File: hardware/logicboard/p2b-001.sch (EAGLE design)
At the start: 70 parts, among them IC1 74LS06N, IC2 4066N, J1 MKR, J2 GPIO, J3 Vcc, J4 RLY, J42 RLY2, J5 SPI, J6 LED, J7 DIN5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

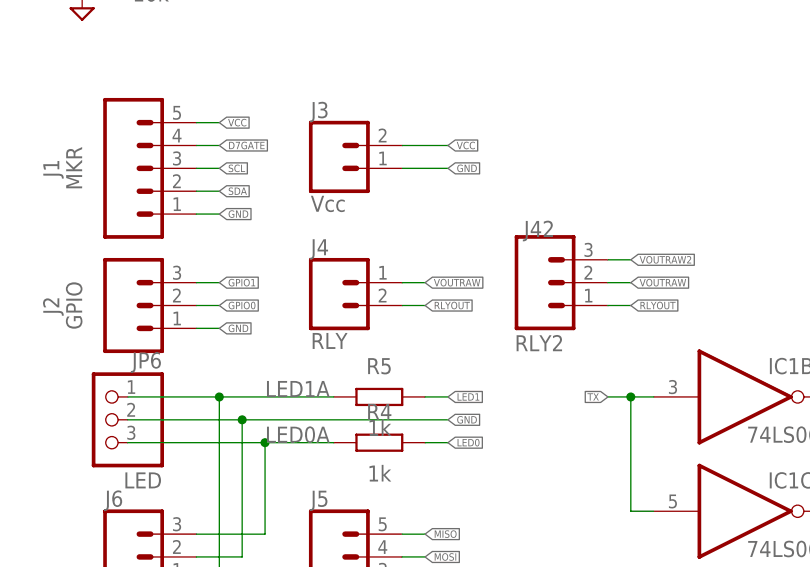
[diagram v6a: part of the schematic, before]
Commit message: J4 is now 3-pin.
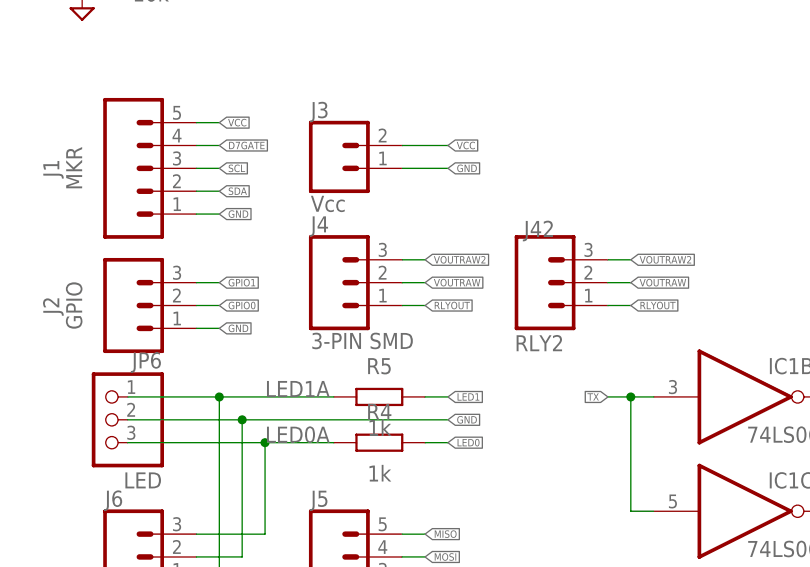
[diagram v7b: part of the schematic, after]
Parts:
- J4: value RLY -> 3-PIN SMD; device SparkFun-Connectors:CONN_02-JST-2MM-SMT -> SparkFun-Connectors:CONN_03JST-SMD
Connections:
- net VOUTRAW2: now also J4.3
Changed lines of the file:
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@@
 <part name="X14" library="wirepad" library_urn="urn:adsk.eagle:library:412" deviceset="PAD-N" device=""/>
 <part name="JP1" library="pinhead" library_urn="urn:adsk.eagle:library:325" deviceset="PINHD-2X3" device="" package3d_urn="urn:adsk.eagle:package:22462/2" value="PWRSEL"/>
-<part name="J4" library="SparkFun-Connectors" library_urn="urn:adsk.eagle:library:513" deviceset="CONN_02" device="-JST-2MM-SMT" package3d_urn="urn:adsk.eagle:package:38042/1" value="RLY"/>
 <part name="J3" library="SparkFun-Connectors" library_urn="urn:adsk.eagle:library:513" deviceset="CONN_02" device="JST-PTH-2" package3d_urn="urn:adsk.eagle:package:38053/1" value="Vcc"/>
 <part name="J5" library="SparkFun-Connectors" library_urn="urn:adsk.eagle:library:513" deviceset="CONN_05" device="JST-VERT" package3d_urn="urn:adsk.eagle:package:38111/1" value="SPI"/>
@@
 <part name="SUPPLY25" library="supply2" library_urn="urn:adsk.eagle:library:372" deviceset="VCC" device=""/>
 <part name="J42" library="SparkFun-Connectors" library_urn="urn:adsk.eagle:library:513" deviceset="CONN_03" device="JST-PTH" package3d_urn="urn:adsk.eagle:package:38069/1" value="RLY2"/>
+<part name="J4" library="SparkFun-Connectors" library_urn="urn:adsk.eagle:library:513" deviceset="CONN_03" device="JST-SMD" package3d_urn="urn:adsk.eagle:package:38075/1" value="3-PIN SMD"/>
 </parts>
 <sheets>
@@
 <attribute name="VALUE" x="77.47" y="226.06" size="1.778" layer="96"/>
 </instance>
-<instance part="J4" gate="G$1" x="88.9" y="48.26" smashed="yes">
-<attribute name="VALUE" x="86.36" y="43.434" size="1.778" layer="96" font="vector"/>
-<attribute name="NAME" x="86.36" y="53.848" size="1.778" layer="95" font="vector"/>
-</instance>
 <instance part="J3" gate="G$1" x="88.9" y="63.5" smashed="yes">
 <attribute name="VALUE" x="86.36" y="58.674" size="1.778" layer="96" font="vector"/>
@@
 <attribute name="VALUE" x="111.76" y="43.18" size="1.778" layer="96" align="bottom-center"/>
 <attribute name="NAME" x="111.76" y="55.88" size="1.778" layer="95" align="bottom-center"/>
+</instance>
+<instance part="J4" gate="J$1" x="88.9" y="50.8" smashed="yes">
+<attribute name="VALUE" x="86.36" y="43.434" size="1.778" layer="96" font="vector"/>
+<attribute name="NAME" x="86.36" y="56.388" size="1.778" layer="95" font="vector"/>
 </instance>
 </instances>
@@
 <pinref part="J42" gate="J$1" pin="3"/>
 </segment>
+<segment>
+<pinref part="J4" gate="J$1" pin="3"/>
+<wire x1="96.52" y1="53.34" x2="99.06" y2="53.34" width="0.1524" layer="91"/>
+<label x="99.06" y="53.34" size="0.8128" layer="95" xref="yes"/>
+</segment>
 </net>
 <net name="VOUT" class="4">
@@
 <wire x1="96.52" y1="50.8" x2="99.06" y2="50.8" width="0.1524" layer="91"/>
 <label x="99.06" y="50.8" size="0.8128" layer="95" xref="yes"/>
-<pinref part="J4" gate="G$1" pin="2"/>
+<pinref part="J4" gate="J$1" pin="2"/>
 </segment>
 <segment>
@@
 <wire x1="96.52" y1="48.26" x2="99.06" y2="48.26" width="0.1524" layer="91"/>
 <label x="99.06" y="48.26" size="0.8128" layer="95" xref="yes"/>
-<pinref part="J4" gate="G$1" pin="1"/>
-</segment>
-<segment>
+<pinref part="J4" gate="J$1" pin="1"/>
+</segment>
+<segment>

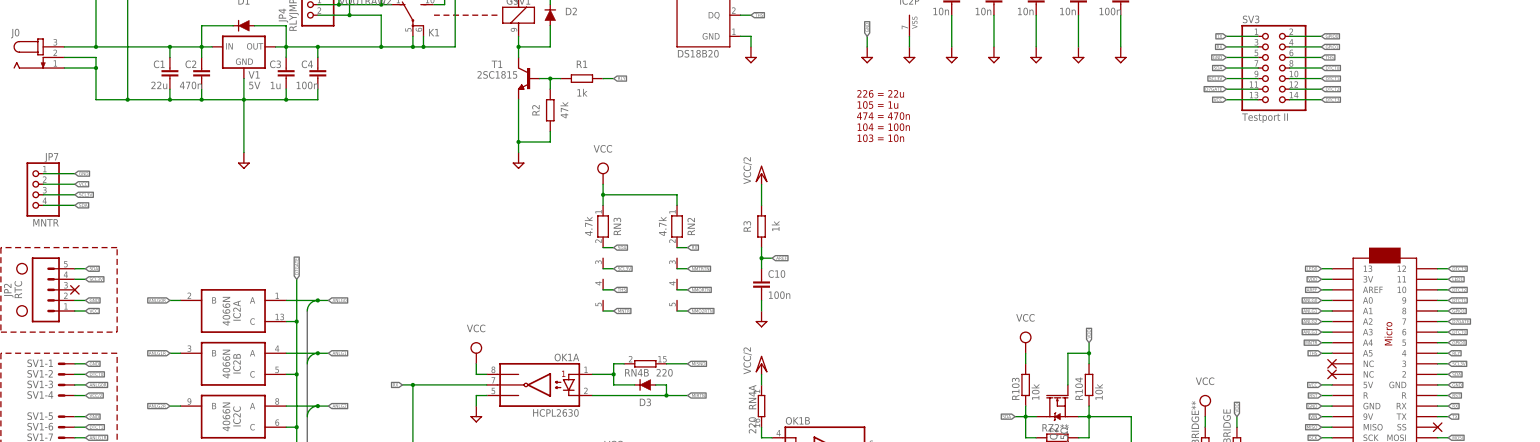
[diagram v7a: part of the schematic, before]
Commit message: Fixed SCL signal.
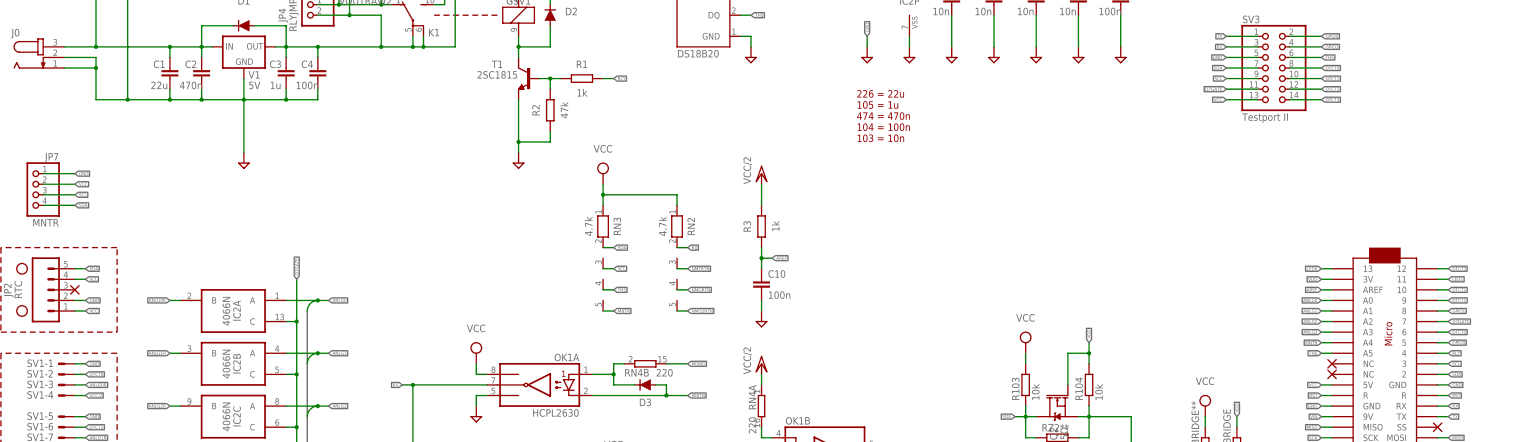
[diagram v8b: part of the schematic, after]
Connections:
- net SCL: now also JP2.4, JP7.3, MC1.3, RN3.3, SV3.9
- net SCL3V: no longer JP2.4, JP7.3, MC1.3, RN3.3, SV3.9
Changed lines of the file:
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@@
-</segment>
-</net>
-<net name="SCL3V" class="0">
-<segment>
-<pinref part="MC1" gate="G$1" pin="3"/>
-<wire x1="368.3" y1="124.46" x2="370.84" y2="124.46" width="0.1524" layer="91"/>
-<label x="370.84" y="124.46" size="0.8128" layer="95" xref="yes"/>
-</segment>
-<segment>
-<pinref part="JP2" gate="G$1" pin="4"/>
-<wire x1="40.64" y1="144.78" x2="43.18" y2="144.78" width="0.1524" layer="91"/>
-<label x="43.18" y="144.78" size="0.8128" layer="95" xref="yes"/>
-</segment>
-<segment>
-<pinref part="RN3" gate="1" pin="3"/>
-<wire x1="167.64" y1="147.32" x2="170.18" y2="147.32" width="0.1524" layer="91"/>
-<label x="170.18" y="147.32" size="0.8128" layer="95" xref="yes"/>
-</segment>
-<segment>
-<pinref part="SV3" gate="A" pin="9"/>
-<wire x1="325.12" y1="193.04" x2="317.5" y2="193.04" width="0.1524" layer="91"/>
-<label x="317.5" y="193.04" size="0.8128" layer="95" rot="R180" xref="yes"/>
-</segment>
-<segment>
-<pinref part="JP7" gate="A" pin="3"/>
-<wire x1="33.02" y1="165.1" x2="40.64" y2="165.1" width="0.1524" layer="91"/>
-<label x="40.64" y="165.1" size="0.8128" layer="95" xref="yes"/>
-</segment>
-<segment>
-<pinref part="Q1" gate="NMOS" pin="S"/>
-<pinref part="R102" gate="G$1" pin="1"/>
-<wire x1="284.48" y1="76.2" x2="281.94" y2="76.2" width="0.1524" layer="91"/>
-<wire x1="284.48" y1="78.74" x2="284.48" y2="76.2" width="0.1524" layer="91"/>
-<junction x="284.48" y="76.2"/>
-<pinref part="RZ1**" gate="G$1" pin="2"/>
-<wire x1="281.94" y1="71.12" x2="284.48" y2="71.12" width="0.1524" layer="91"/>
-<wire x1="284.48" y1="71.12" x2="284.48" y2="76.2" width="0.1524" layer="91"/>
-<pinref part="LCD1" gate="G$1" pin="8"/>
-<wire x1="358.14" y1="76.2" x2="284.48" y2="76.2" width="0.1524" layer="91"/>
-<label x="345.44" y="76.2" size="1.778" layer="95"/>
 </segment>
 </net>
@@
 <label x="76.2" y="63.5" size="0.8128" layer="95" xref="yes"/>
 </segment>
+<segment>
+<pinref part="MC1" gate="G$1" pin="3"/>
+<wire x1="368.3" y1="124.46" x2="370.84" y2="124.46" width="0.1524" layer="91"/>
+<label x="370.84" y="124.46" size="0.8128" layer="95" xref="yes"/>
+</segment>
+<segment>
+<pinref part="JP2" gate="G$1" pin="4"/>
+<wire x1="40.64" y1="144.78" x2="43.18" y2="144.78" width="0.1524" layer="91"/>
+<label x="43.18" y="144.78" size="0.8128" layer="95" xref="yes"/>
+</segment>
+<segment>
+<pinref part="RN3" gate="1" pin="3"/>
+<wire x1="167.64" y1="147.32" x2="170.18" y2="147.32" width="0.1524" layer="91"/>
+<label x="170.18" y="147.32" size="0.8128" layer="95" xref="yes"/>
+</segment>
+<segment>
+<pinref part="SV3" gate="A" pin="9"/>
+<wire x1="325.12" y1="193.04" x2="317.5" y2="193.04" width="0.1524" layer="91"/>
+<label x="317.5" y="193.04" size="0.8128" layer="95" rot="R180" xref="yes"/>
+</segment>
+<segment>
+<pinref part="JP7" gate="A" pin="3"/>
+<wire x1="33.02" y1="165.1" x2="40.64" y2="165.1" width="0.1524" layer="91"/>
+<label x="40.64" y="165.1" size="0.8128" layer="95" xref="yes"/>
+</segment>
 </net>
 <net name="SDA3V" class="0">
@@
 </segment>
 </net>
+<net name="SCL3V" class="0">
+<segment>
+<pinref part="Q1" gate="NMOS" pin="S"/>
+<pinref part="R102" gate="G$1" pin="1"/>
+<wire x1="284.48" y1="76.2" x2="281.94" y2="76.2" width="0.1524" layer="91"/>
+<wire x1="284.48" y1="78.74" x2="284.48" y2="76.2" width="0.1524" layer="91"/>
+<junction x="284.48" y="76.2"/>
+<pinref part="RZ1**" gate="G$1" pin="2"/>
+<wire x1="281.94" y1="71.12" x2="284.48" y2="71.12" width="0.1524" layer="91"/>
+<wire x1="284.48" y1="71.12" x2="284.48" y2="76.2" width="0.1524" layer="91"/>
+<pinref part="LCD1" gate="G$1" pin="8"/>
+<wire x1="358.14" y1="76.2" x2="284.48" y2="76.2" width="0.1524" layer="91"/>
+<label x="345.44" y="76.2" size="1.778" layer="95"/>
+</segment>
+</net>
